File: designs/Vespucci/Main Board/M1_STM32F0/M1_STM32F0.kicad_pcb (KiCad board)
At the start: 4 copper layers, 131.3 x 20.3 mm, 52 parts, among them J1 PCIe Connector, J2 PCIe Connector, J3 PCIe Connector, J5 PCIe Connector, J6 PCIe Card Edge, J7 Screw_Terminal_01x02, Q1 BSS138W, SW1 SW_Push, U1 NL17SZ00, U2 NL17SZ00, U3 STM32F070RBTx, U4 NL17SZ00, U5 NL17SZ00, U6 AP6320x

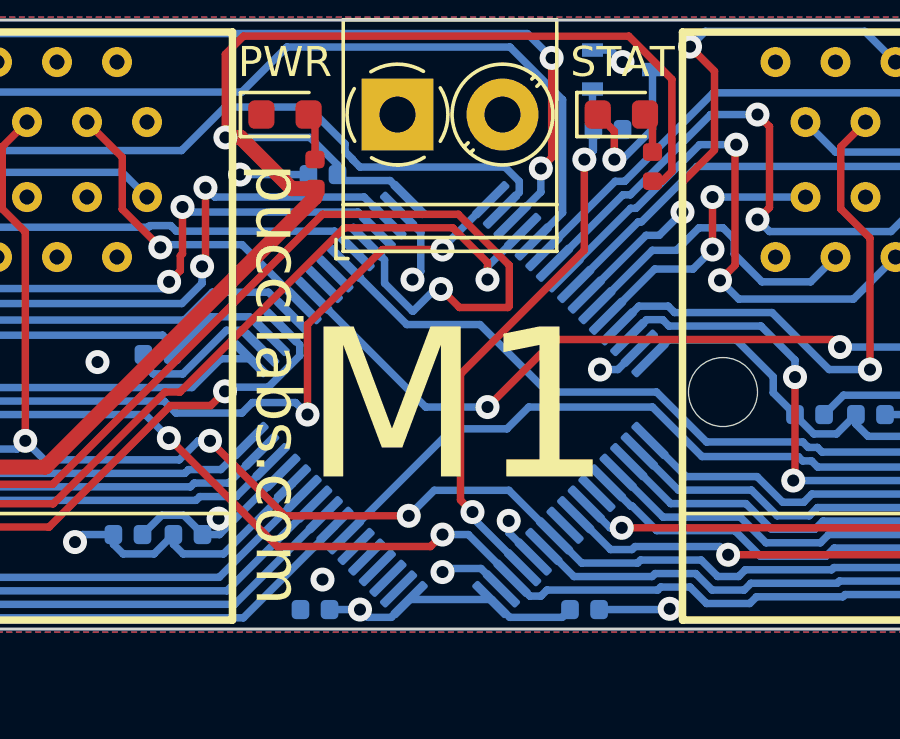
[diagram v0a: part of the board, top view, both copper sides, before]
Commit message: Move Vespucci and add adc array
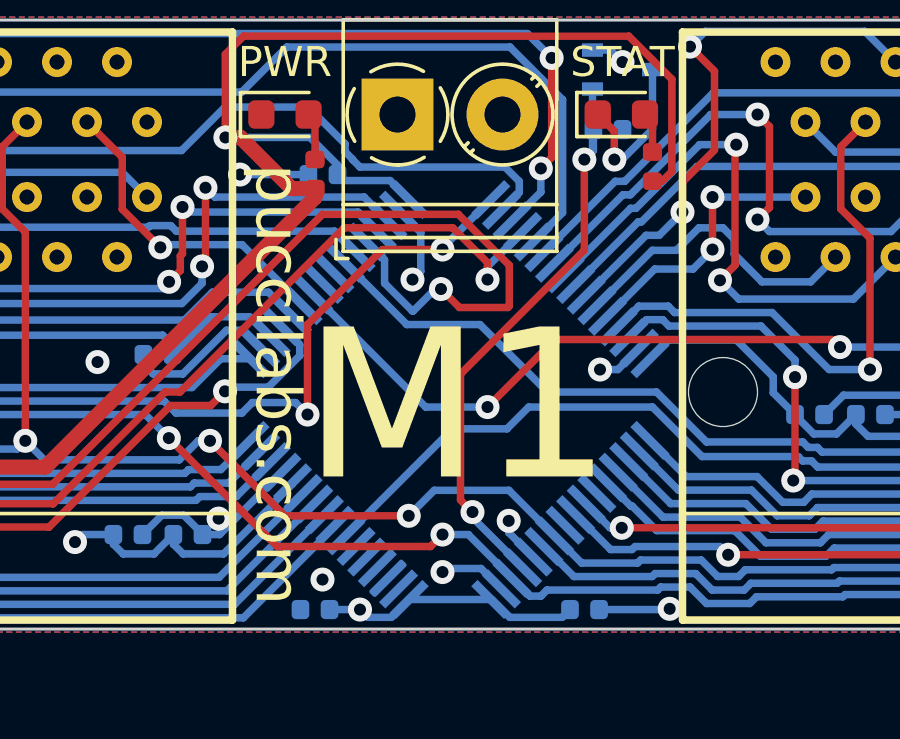
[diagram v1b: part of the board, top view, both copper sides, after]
